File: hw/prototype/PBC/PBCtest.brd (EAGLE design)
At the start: 50 x 50 mm, 13 parts, among them IC1 7812L, U1 TC4427EOA

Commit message: tracing
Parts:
- removed U$4: (no value), ultrasonic:TCT40-16
- added T2: (no value), ultrasonic:TCT40-16
- moved D1 24.9 mm to (7.15, 27.5), flipped to the bottom, turned to 90 degrees
- moved SVJ8 17.7 mm to (19.9, 43.9), flipped to the bottom, turned to 180 degrees
- moved IC1 13.0 mm to (13.0, 28.8), flipped to the bottom, turned to 270 degrees
- moved S1 11.1 mm to (33.6, 36.5), flipped to the bottom, turned to 0 degrees
- moved C66 9.78 mm to (19.7, 35.6), flipped to the bottom, turned to 0 degrees
- moved J1 7.07 mm to (8.88, 39.5), flipped to the bottom, turned to 270 degrees
- moved C65 5.53 mm to (17.2, 28.8), flipped to the bottom, turned to 90 degrees
- moved C33 5.45 mm to (18.4, 19.4), turned to 0 degrees
- moved U1 5.34 mm to (25.4, 18.4)
- moved SVI10 3.61 mm to (44.0, 35.7), flipped to the bottom
- moved C1 1.09 mm to (18.5, 16.3), turned to 0 degrees
- flipped T1 to the bottom
- renumbered U$3 to T1
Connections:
- net GND: now also T2.P1; no longer U$4.P1
- net PA6: now also U1.4; no longer U1.2
- net PA7: now also U1.2; no longer U1.4
- net PD6: now also T2.P0; no longer U$4.P0
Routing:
- net V20: track 78.0 -> 47.8 mm
- net VIN: track 6.24 -> 27.7 mm
- net PD7: track 19.0 -> 6.07 mm
- net PA7: track 30.3 -> 20.8 mm
- net GND: track 8.73 -> 0.00 mm
- net N$4: track 14.3 -> 21.9 mm
- net PD6: track 12.0 -> 6.12 mm
- net PA6: track 28.0 -> 24.4 mm
- net RESET: track 13.5 -> 14.6 mm
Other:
- board text added: "18VDC"
- board text added: "3V3"
- board text added: "5V"
- board text added: "BOTTOM LAYER"
- board text added: "GND"
- board text added: "OFF"
- board text added: "ON"
- board text added: "PWR_IN"
- board text added: "RESET"
- board text added: "T1"
- board text added: "T2"
- board text added: "TOP LAYER"
- board text added: "VIN"

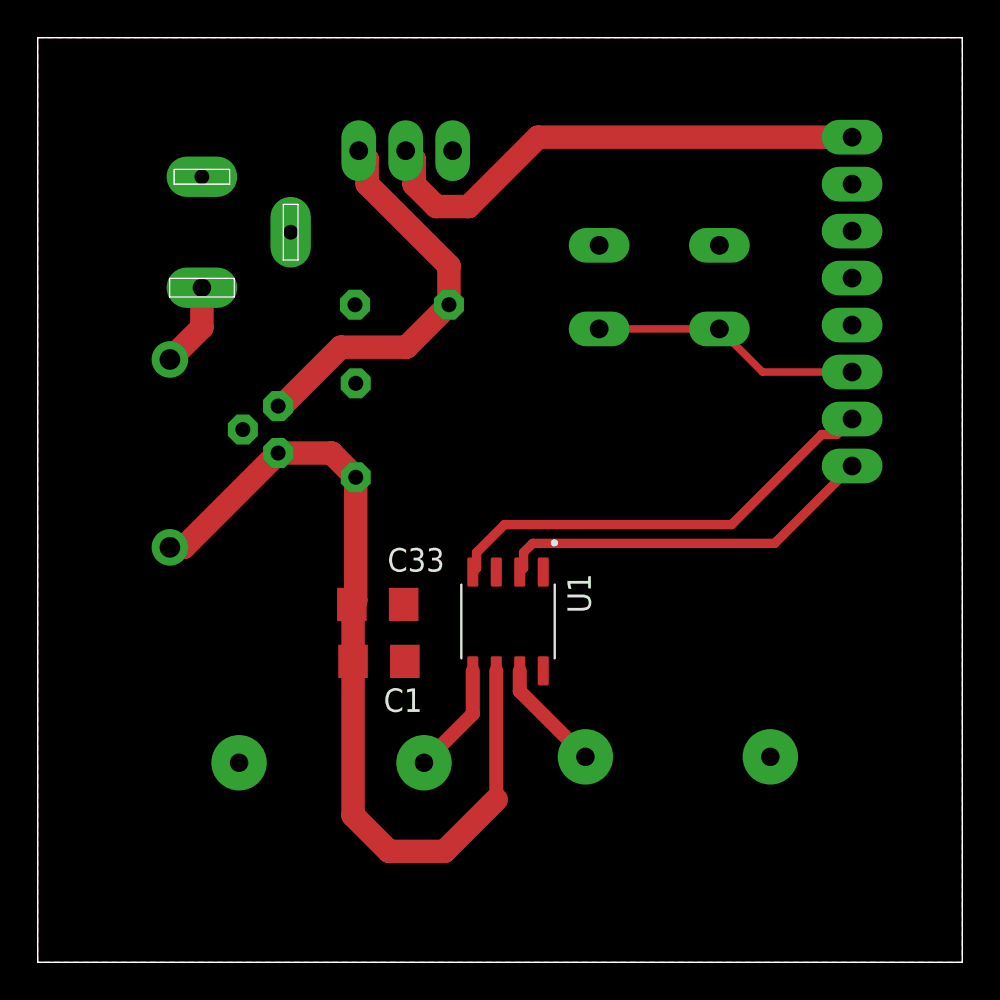
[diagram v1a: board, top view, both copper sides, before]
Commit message: Board design enhancments
* New alignment marks
* Increased thermal isolation to 20mil
* Upgraded PCBtest to new design rules with 20mil clearance and increased text size to test the same object sizes of the main board
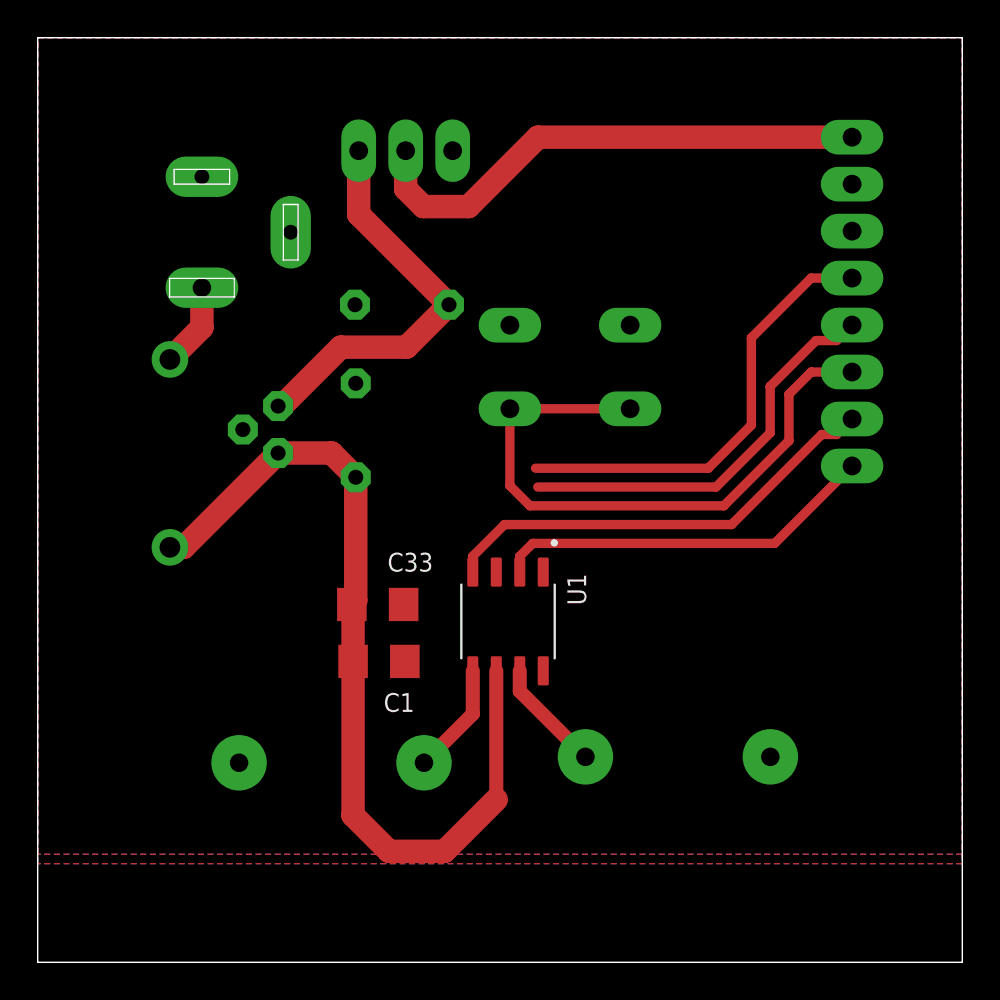
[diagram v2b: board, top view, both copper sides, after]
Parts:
- moved S1 6.48 mm to (28.8, 32.2)
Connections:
- new net N$2: SVI10.5
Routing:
- net 5V: track 0.00 -> 24.1 mm
- net N$2: track 0.00 -> 22.1 mm
- net RESET: track 14.6 -> 34.1 mm
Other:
- board text added: "(1,1)"
- board text added: "(2,1)"
- board text added: "27"
- board text added: "29"
- board text added: "PCBtest v1.1"
- board text added: "VIN_EN"
- board text added: "bottom"
- board text added: "top"
- board text removed: "BOTTOM LAYER"
- board text removed: "PCBtest v1.0"
- board text removed: "PWR_IN"
- board text removed: "TOP LAYER"
